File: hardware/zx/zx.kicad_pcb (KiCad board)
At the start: 2 copper layers, 71.6 x 59.9 mm, 51 parts, among them J1 ZX Keyboard, J10 Conn_01x01, J11 Conn_01x01, J12 Conn_01x01, J13 Conn_01x01, J14 Conn_01x01, J15 Conn_01x01, J16 Conn_01x01, J17 Conn_01x01, J18 Conn_01x01, J19 Conn_01x01, J2 GOTEK, J20 Conn_01x01, J21 Conn_01x01, J22 Conn_01x01, J23 Conn_01x01, J24 Conn_01x01, J25 Conn_01x01, J26 Conn_01x01, J27 Conn_01x01, J28 Conn_01x01, J29 Conn_01x01, J3 UART, J30 Conn_01x01, J4 USB_A, J5 USB_A, J6 Keyboard, J7 Mouse, J8 Kempston Mouse, J9 Z80, SW1 RESET, SW2 BOOT0, SW3 BOOT1, U1 CH559L, U2 CH446Q, Y1 12MHz

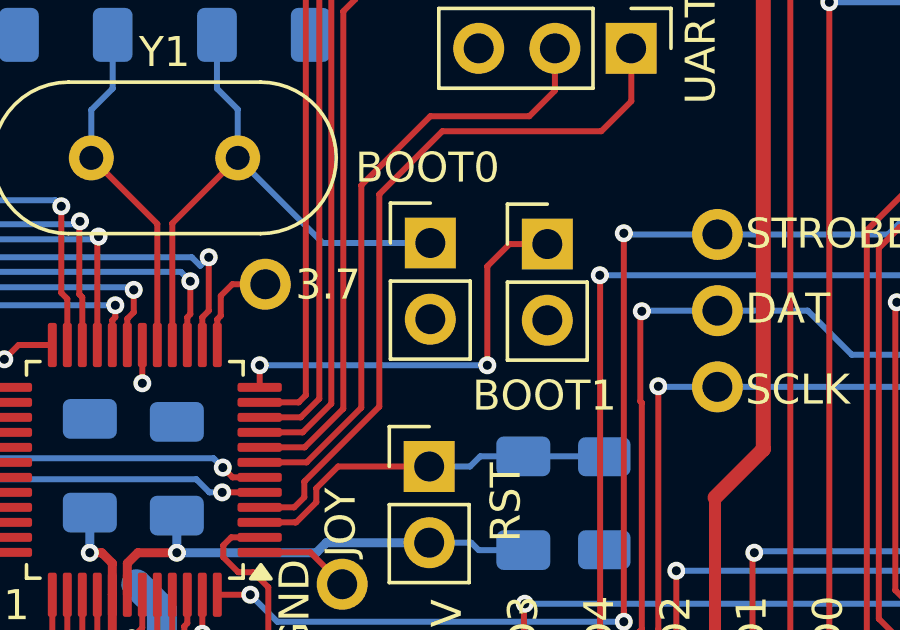
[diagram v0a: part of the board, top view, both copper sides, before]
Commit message: Remove BOOT1 switch from schematic. Correct LED polarity.
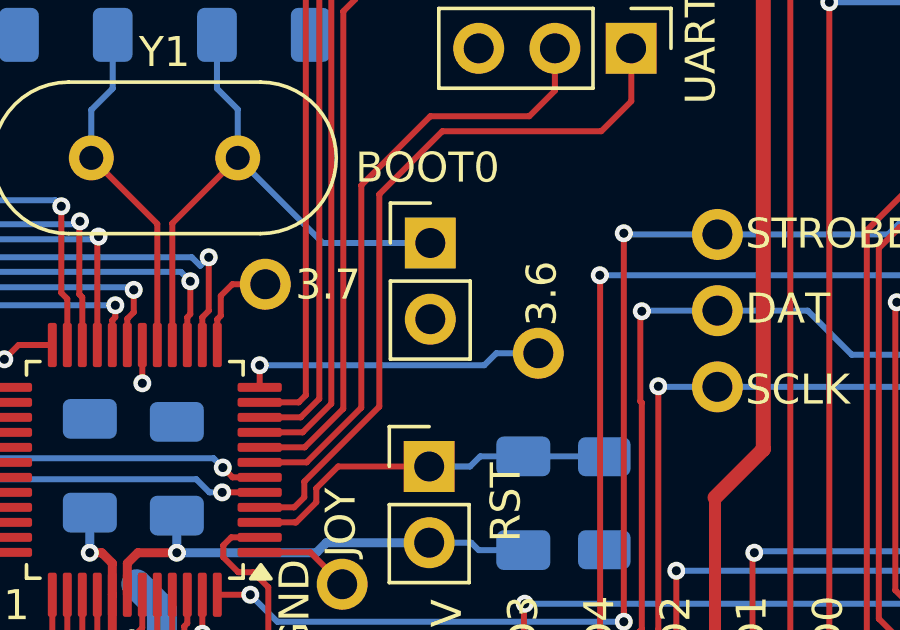
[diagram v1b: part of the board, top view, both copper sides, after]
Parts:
- removed SW3: BOOT1, Connector_PinHeader_2.54mm:PinHeader_1x02_P2.54mm_Vertical
- added J31: Conn_01x01, THT_Pin:THT_Pin_Vertical, F.Cu at (135.0, 133.5)
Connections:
- D1 pad 1: /P1_7 -> Net-(D1-K)
- D1 pad 2: Net-(D1-A) -> /P1_7
- R5 pad 1: Net-(D1-A) -> Net-(D1-K)
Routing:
- net Net-(D1-A): track 5.45 -> 0.00 mm, vias 1 -> 0
- net /P1_7: track 14.0 -> 19.4 mm, vias 2 -> 3
- net /P3_6: track 13.9 -> 10.2 mm, vias 2 -> 1
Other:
- board text added: "3.6"
- board text removed: "BOOT1"

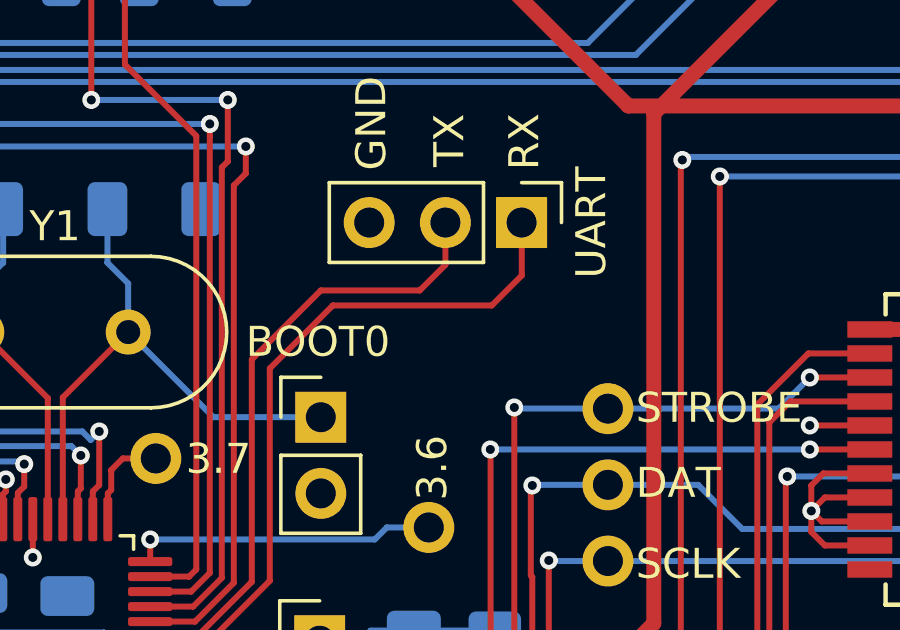
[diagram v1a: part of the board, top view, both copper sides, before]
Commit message: Prototype board: Fixed Help screen with Gluk Reset Service after power on. Add 10K pulldown resistor for STB signal, init P1 value before setting port to output.
Fix not required for ZX BUS / CPLD implementation because of rising_edge of STB signal used instead of active high level.
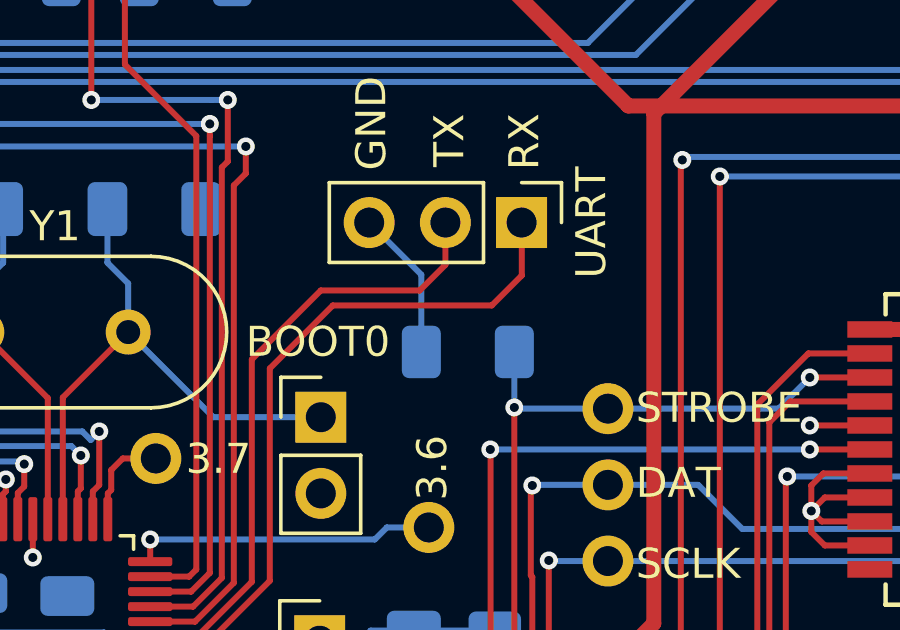
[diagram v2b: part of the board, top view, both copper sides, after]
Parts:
- added R6: 10K, Resistor_SMD:R_1206_3216Metric_Pad1.30x1.75mm_HandSolder, B.Cu at (136.3, 127.7)
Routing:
- net GND: track 47.1 -> 52.1 mm
- net /STROBE: track 39.2 -> 41.0 mm
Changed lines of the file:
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@@
 		)
 	)
+	(footprint "Resistor_SMD:R_1206_3216Metric_Pad1.30x1.75mm_HandSolder"
+		(layer "B.Cu")
+		(at 136.3 127.65 180)
+		(descr "Resistor SMD 1206 (3216 Metric), square (rectangular) end terminal, IPC_7351 nominal with elongated pad for handsoldering. (Body size source: IPC-SM-782 page 72, https://www.pcb-3d.com/wordpress/wp-content/uploads/ipc-sm-782a_amendment_1_and_2.pdf), generated with kicad-footprint-generator")
+		(tags "resistor handsolder")
+		(property "Reference" "R6"
+			(at 0 1.82 180)
+			(layer "B.SilkS")
+			(effects
+				(font
+					(size 1 1)
+					(thickness 0.15)
+				)
+				(justify mirror)
+			)
+		)
+		(property "Value" "10K"
+			(at 0 -1.82 180)
+			(layer "B.Fab")
+			(effects
+				(font
+					(size 1 1)
+					(thickness 0.15)
+				)
+				(justify mirror)
+			)
+		)
+		(property "Footprint" "Resistor_SMD:R_1206_3216Metric_Pad1.30x1.75mm_HandSolder"
+			(at 0 0 0)
+			(unlocked yes)
+			(layer "B.Fab")
+			(hide yes)
+			(effects
+				(font
+					(size 1.27 1.27)
+				)
+				(justify mirror)
+			)
+		)
+		(property "Datasheet" ""
+			(at 0 0 0)
+			(unlocked yes)
+			(layer "B.Fab")
+			(hide yes)
+			(effects
+				(font
+					(size 1.27 1.27)
+				)
+				(justify mirror)
+			)
+		)
+		(property "Description" "Resistor"
+			(at 0 0 0)
+			(unlocked yes)
+			(layer "B.Fab")
+			(hide yes)
+			(effects
+				(font
+					(size 1.27 1.27)
+				)
+				(justify mirror)
+			)
+		)
+		(property ki_fp_filters "R_*")
+		(sheetname "Root")
+		(sheetfile "zx.kicad_sch")
+		(attr smd)
+		(fp_line
+			(start 0.727064 0.91)
+			(end -0.727064 0.91)
+			(stroke
+				(width 0.12)
+				(type solid)
+			)
+			(layer "B.SilkS")
+		)
+		(fp_line
+			(start 0.727064 -0.91)
+			(end -0.727064 -0.91)
+			(stroke
+				(width 0.12)
+				(type solid)
+			)
+			(layer "B.SilkS")
+		)
+		(fp_line
+			(start 2.45 1.12)
+			(end -2.45 1.12)
+			(stroke
+				(width 0.05)
+				(type solid)
+			)
+			(layer "B.CrtYd")
+		)
+		(fp_line
+			(start 2.45 -1.12)
+			(end 2.45 1.12)
+			(stroke
+				(width 0.05)
+				(type solid)
+			)
+			(layer "B.CrtYd")
+		)
+		(fp_line
+			(start -2.45 1.12)
+			(end -2.45 -1.12)
+			(stroke
+				(width 0.05)
+				(type solid)
+			)
+			(layer "B.CrtYd")
+		)
+		(fp_line
+			(start -2.45 -1.12)
+			(end 2.45 -1.12)
+			(stroke
+				(width 0.05)
+				(type solid)
+			)
+			(layer "B.CrtYd")
+		)
+		(fp_line
+			(start 1.6 0.8)
+			(end -1.6 0.8)
+			(stroke
+				(width 0.1)
+				(type solid)
+			)
+			(layer "B.Fab")
+		)
+		(fp_line
+			(start 1.6 -0.8)
+			(end 1.6 0.8)
+			(stroke
+				(width 0.1)
+				(type solid)
+			)
+			(layer "B.Fab")
+		)
+		(fp_line
+			(start -1.6 0.8)
+			(end -1.6 -0.8)
+			(stroke
+				(width 0.1)
+				(type solid)
+			)
+			(layer "B.Fab")
+		)
+		(fp_line
+			(start -1.6 -0.8)
+			(end 1.6 -0.8)
+			(stroke
+				(width 0.1)
+				(type solid)
+			)
+			(layer "B.Fab")
+		)
+		(fp_text user "${REFERENCE}"
+			(at 0 0 180)
+			(layer "B.Fab")
+			(effects
+				(font
+					(size 0.8 0.8)
+					(thickness 0.12)
+				)
+				(justify mirror)
+			)
+		)
+		(pad "1" smd roundrect
+			(at -1.55 0 180)
+			(size 1.3 1.75)
+			(layers "B.Cu" "B.Paste" "B.Mask")
+			(roundrect_rratio 0.192308)
+			(net 69 "/STROBE")
+			(pintype "passive")
+		)
+		(pad "2" smd roundrect
+			(at 1.55 0 180)
+			(size 1.3 1.75)
+			(layers "B.Cu" "B.Paste" "B.Mask")
+			(roundrect_rratio 0.192308)
+			(net 3 "GND")
+			(pintype "passive")
+		)
+		(model "${KICAD8_3DMODEL_DIR}/Resistor_SMD.3dshapes/R_1206_3216Metric.wrl"
+			(offset
+				(xyz 0 0 0)
+			)
+			(scale
+				(xyz 1 1 1)
+			)
+			(rotate
+				(xyz 0 0 0)
+			)
+		)
+	)
 	(footprint "Capacitor_SMD:C_1206_3216Metric_Pad1.33x1.80mm_HandSolder"
 		(layer "B.Cu")
@@
 	)
 	(segment
+		(start 134.75 127.65)
+		(end 134.75 125.07325)
+		(width 0.2)
+		(layer "B.Cu")
+		(net 3)
+	)
+	(segment
 		(start 123.55 144.45)
 		(end 122.45 143.35)
@@
 	)
 	(segment
+		(start 134.75 125.07325)
+		(end 133.013018 123.336268)
+		(width 0.2)
+		(layer "B.Cu")
+		(net 3)
+	)
+	(segment
 		(start 125.9 145)
 		(end 125.35 144.45)
@@
 		(width 0.2)
 		(layer "B.Cu")
+		(net 69)
+	)
+	(segment
+		(start 137.85 129.5)
+		(end 137.85 127.65)
+		(width 0.2)
+		(layer "B.Cu")
